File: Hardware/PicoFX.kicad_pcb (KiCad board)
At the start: 4 copper layers, 59 x 95 mm, 102 parts, among them J1 RPI_ADC, J2 RP_GPIO, U1 AMS1117-5.0, U2 AMS1117-3.3, U3 MCP6002-xSN, U4 MCP6002-xSN, U5 CS4272, X1 PEDAL_COMBO_TOP

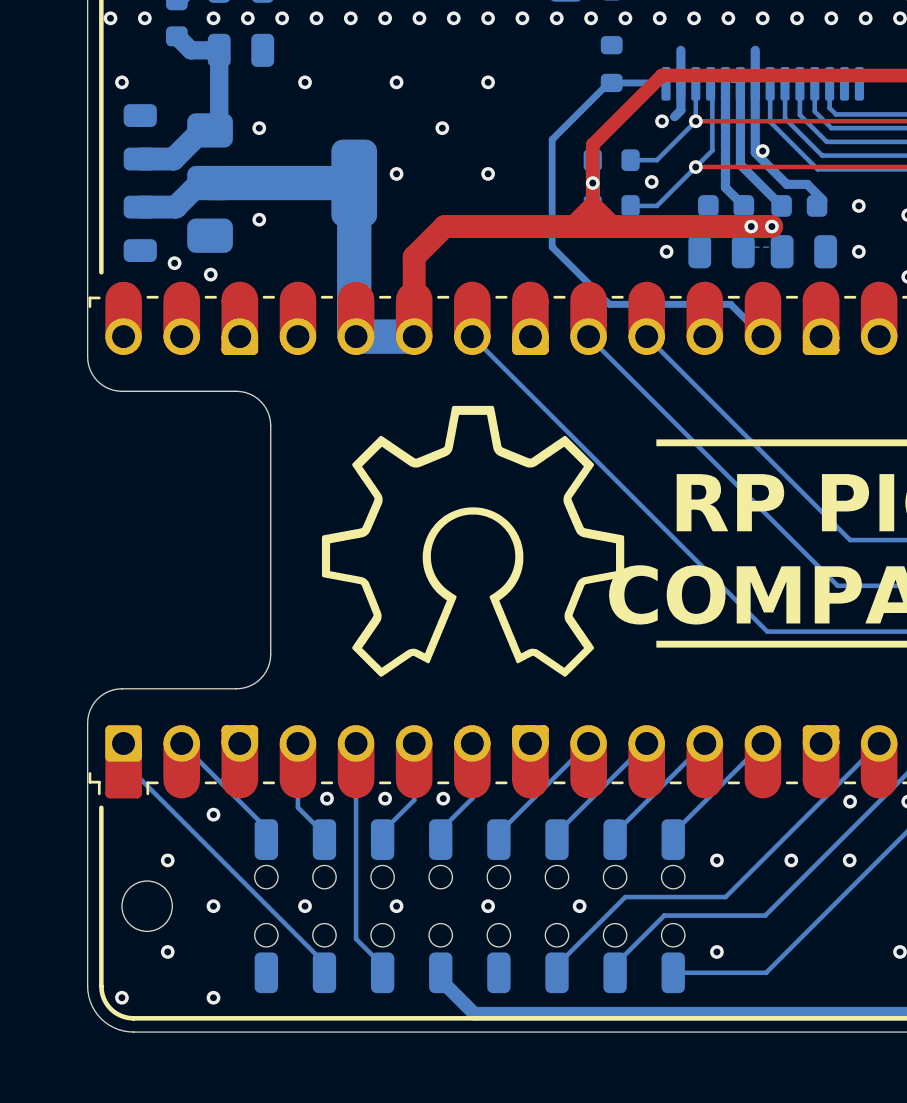
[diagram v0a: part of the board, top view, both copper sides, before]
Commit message: Layout revision
Minor updated to references.
Minor updated to the PCB layout.
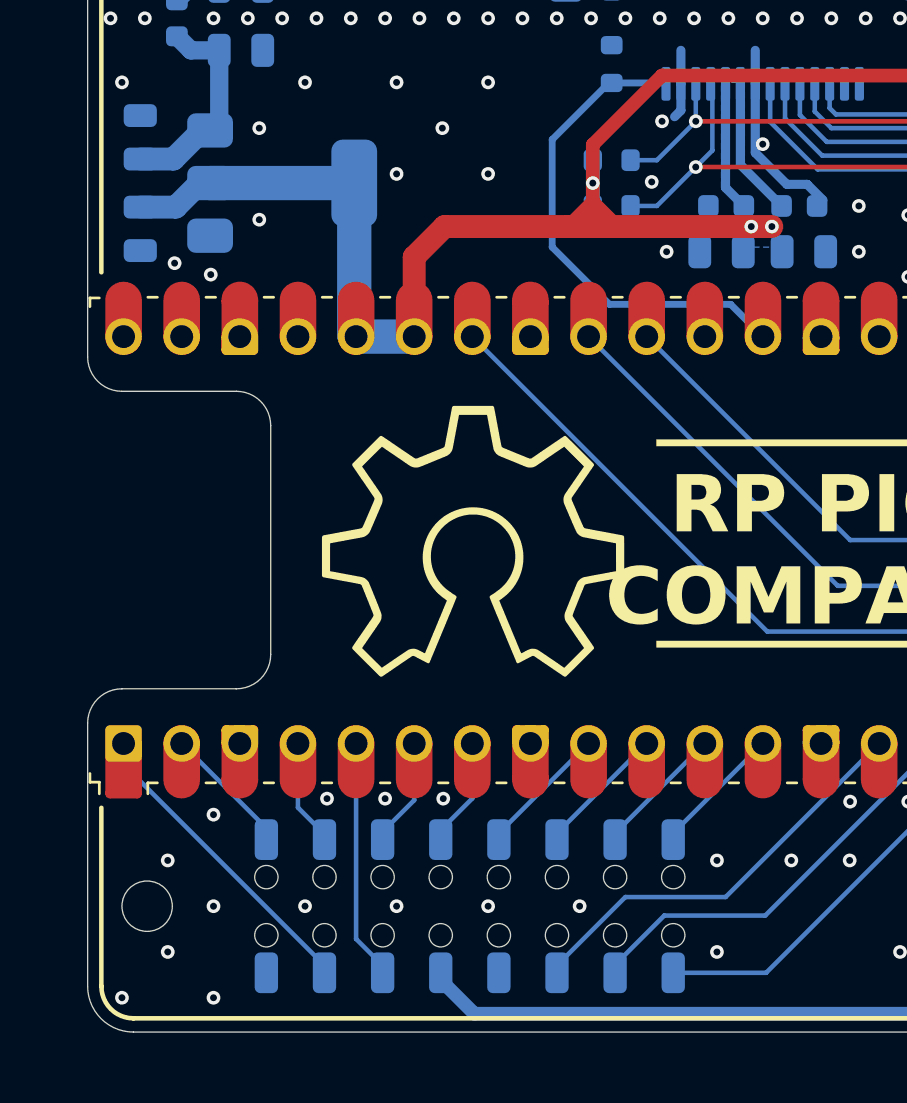
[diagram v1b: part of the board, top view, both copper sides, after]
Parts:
- renumbered C8 to C10, C7 to C11, C9 to C12, C42 to C13, C10 to C14, C11 to C15, C12 to C16, C13 to C17, C14 to C18, C15 to C19, C41 to C2, C16 to C20, C17 to C21, C18 to C22, C19 to C23, C20 to C24, C21 to C25, C22 to C26, C23 to C27, C24 to C28, C25 to C29, C2 to C3, C26 to C30, C27 to C31, C28 to C32, C29 to C33, C30 to C34, C31 to C35, C32 to C36, C33 to C37, C34 to C38, C35 to C39, C3 to C4, C36 to C40, C37 to C41, C38 to C42, C4 to C5, C5 to C6, C39 to C7, C6 to C8, C40 to C9, FB3 to FB2, FB2 to FB3, H7 to H4, H9 to H5, H8 to H6, H10 to H7
